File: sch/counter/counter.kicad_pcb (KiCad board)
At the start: 2 copper layers, 206 parts, among them J1 Q1, J10 ~CLK, J11 ~RST, J12 Cout, J13 ~Cout, J14 Vcc, J15 GND, J2 ~Q1, J3 Q2, J4 ~Q2, J5 Q4, J6 ~Q4, J7 Q8, J8 ~Q8, J9 CLK, Q1 Q_NMOS_GSD, Q10 Q_NMOS_GSD, Q11 Q_NMOS_GSD, Q12 Q_NMOS_GSD, Q13 Q_NMOS_GSD, Q14 Q_NMOS_GSD, Q15 Q_NMOS_GSD, Q16 Q_NMOS_GSD, Q17 Q_NMOS_GSD, Q18 Q_NMOS_GSD, Q19 Q_NMOS_GSD, Q2 Q_NMOS_GSD, Q20 Q_NMOS_GSD, Q21 Q_NMOS_GSD, Q22 Q_NMOS_GSD, Q23 Q_NMOS_GSD, Q24 Q_NMOS_GSD, Q25 Q_NMOS_GSD, Q26 Q_NMOS_GSD, Q27 Q_NMOS_GSD, Q28 Q_NMOS_GSD, Q29 Q_NMOS_GSD, Q3 Q_NMOS_GSD, Q30 Q_NMOS_GSD, Q31 Q_NMOS_GSD, Q32 Q_NMOS_GSD, Q33 Q_NMOS_GSD, Q34 Q_NMOS_GSD, Q35 Q_NMOS_GSD, Q4 Q_NMOS_GSD, Q5 Q_NMOS_GSD, Q6 Q_NMOS_GSD, Q7 Q_NMOS_GSD, Q8 Q_NMOS_GSD, Q9 Q_NMOS_GSD

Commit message: The counter board is complete
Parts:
- removed D93, D94, D95, D96: D, Diode_SMD:D_MiniMELF
- removed JP1, JP2, JP3, JP4: Jumper_3_Open, Connector_PinHeader_2.54mm:PinHeader_1x03_P2.54mm_Vertical
- added REF**: MountingHole_3.2mm_M3_DIN965_Pad, MountingHole:MountingHole_3.2mm_M3_DIN965_Pad, F.Cu at (149.0, 112.0)
- added REF**: MountingHole_3.2mm_M3_DIN965_Pad, MountingHole:MountingHole_3.2mm_M3_DIN965_Pad, F.Cu at (149.0, 29.0)
- added REF**: MountingHole_3.2mm_M3_DIN965_Pad, MountingHole:MountingHole_3.2mm_M3_DIN965_Pad, F.Cu at (104.0, 29.0)
- added REF**: MountingHole_3.2mm_M3_DIN965_Pad, MountingHole:MountingHole_3.2mm_M3_DIN965_Pad, F.Cu at (104.0, 112.0)
- moved Q33 304.7 mm to (113.3, 110.7)
- moved D98 300.0 mm to (118.4, 112.5)
- moved D97 299.4 mm to (118.4, 109.7)
- moved D87 298.6 mm to (113.8, 105.4), turned to 270 degrees
- moved D88 296.3 mm to (111.3, 105.4), turned to 270 degrees
- moved D86 296.1 mm to (106.2, 105.4), turned to 270 degrees
- moved D90 295.6 mm to (116.3, 105.4), turned to 270 degrees
- moved D89 293.3 mm to (118.9, 105.4), turned to 270 degrees
- moved D92 291.5 mm to (121.4, 105.4), turned to 270 degrees
- moved D85 288.0 mm to (108.7, 105.4), turned to 270 degrees
- moved R37 285.6 mm to (126.2, 106.2), turned to 270 degrees
- moved D49 281.0 mm to (104.1, 78.7)
- moved R22 279.0 mm to (108.6, 77.5), turned to 180 degrees
- moved R30 279.0 mm to (108.6, 95.2), turned to 180 degrees
- moved D91 278.2 mm to (124.0, 105.4), turned to 270 degrees
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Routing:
- net GND: track 0.00 -> 379.2 mm, vias 0 -> 36
- net VCC: track 0.00 -> 374.1 mm, vias 0 -> 37
- net /~ARST: track 0.00 -> 316.4 mm, vias 0 -> 21
- net /~Q1: track 26.7 -> 233.8 mm, vias 0 -> 5
- net /Q1: track 9.15 -> 211.5 mm, vias 0 -> 3
- net /~Q2: track 0.00 -> 198.9 mm, vias 0 -> 5
- net /Q2: track 0.00 -> 184.5 mm, vias 0 -> 3
- net /~Q4: track 0.00 -> 168.6 mm, vias 0 -> 5
- net /Q4: track 0.00 -> 159.2 mm, vias 0 -> 3
- net /~Q8: track 0.00 -> 111.2 mm, vias 0 -> 3
- net /Q8: track 0.00 -> 85.2 mm
- net Net-(D71-Pad1): track 0.00 -> 26.5 mm
- net Net-(C3-Pad1): track 0.00 -> 26.5 mm
- net Net-(D31-Pad1): track 0.00 -> 26.4 mm
- net Net-(D51-Pad1): track 0.00 -> 25.9 mm
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- added copper zone on F.Cu, net GND
- added copper zone on B.Cu, net VCC
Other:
- net class Default: clearance 0.2 -> 0.25
- rule trace_clearance: 0.2 -> 0.25

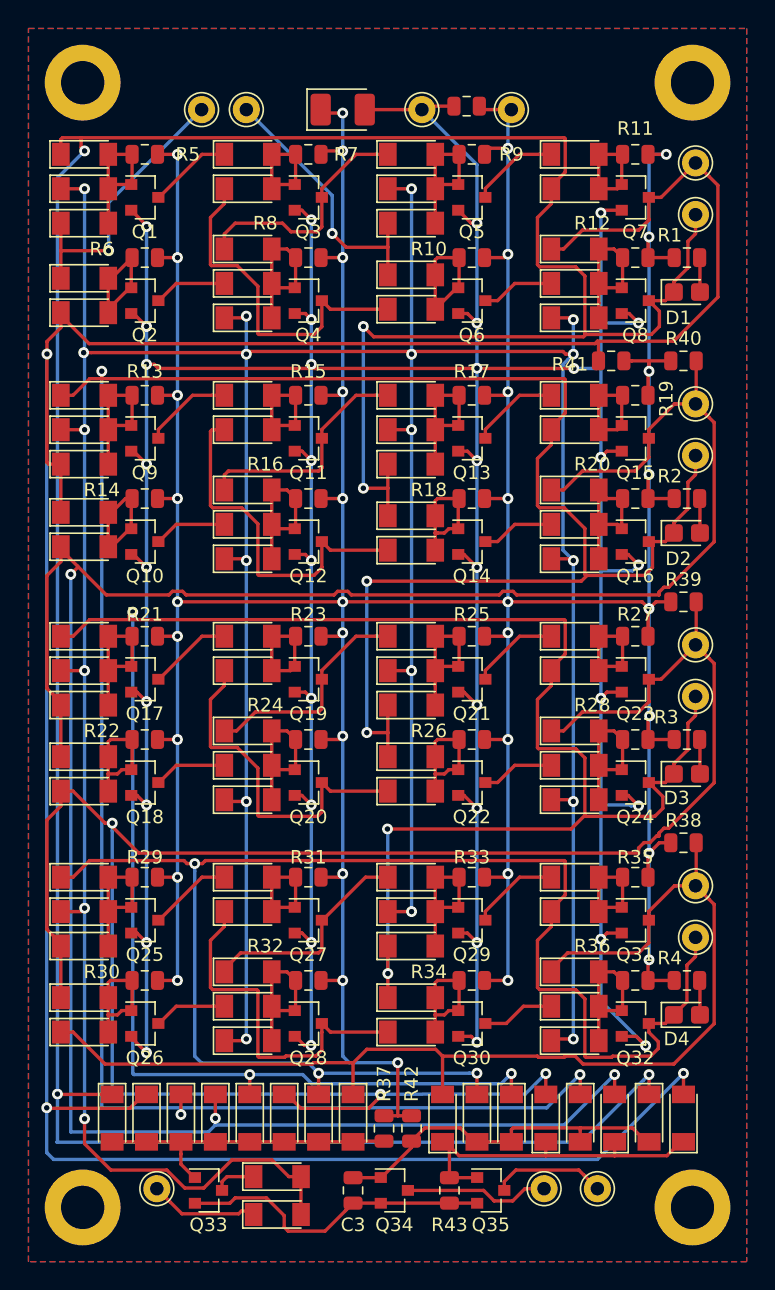
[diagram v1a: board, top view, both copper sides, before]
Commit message: Board modified: connectors used
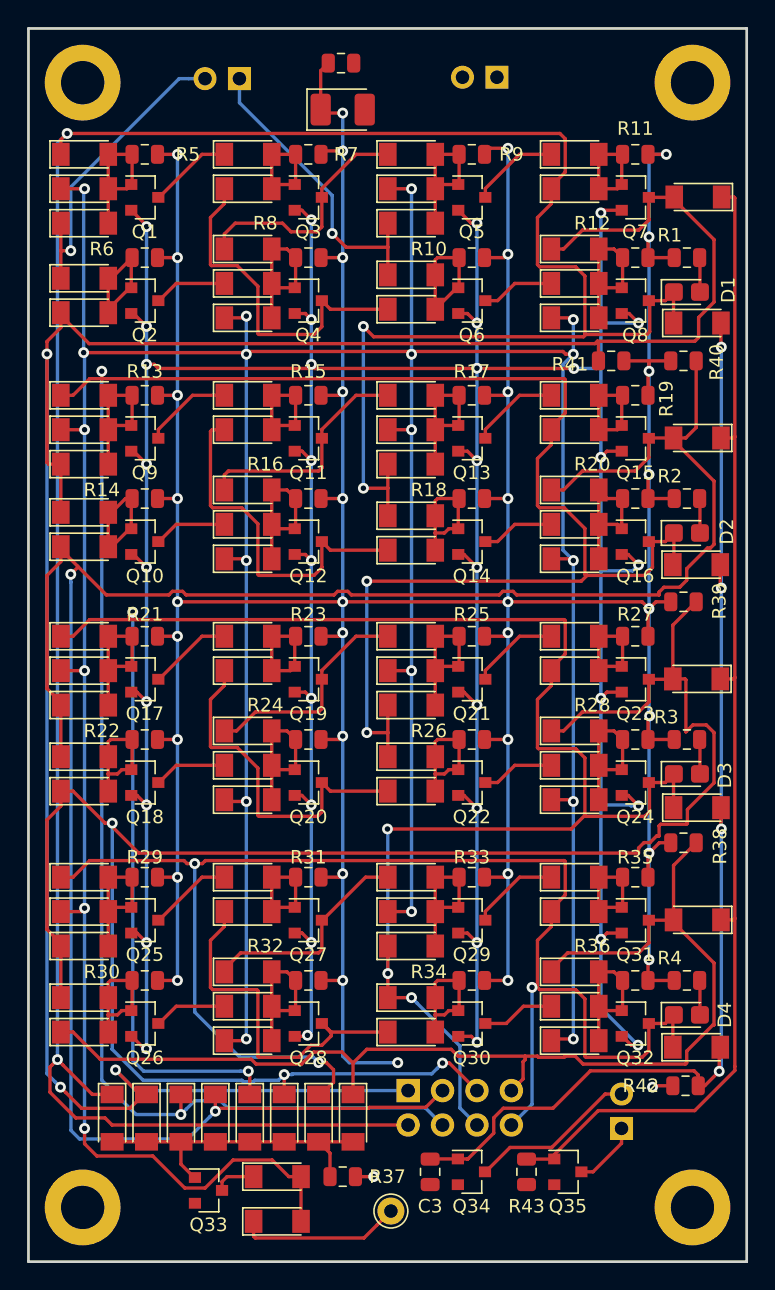
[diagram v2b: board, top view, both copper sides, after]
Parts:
- removed J10: ~CLK, Connector_Pin:Pin_D1.0mm_L10.0mm
- removed J12: Cout, Connector_Pin:Pin_D1.0mm_L10.0mm
- removed J13: ~Cout, Connector_Pin:Pin_D1.0mm_L10.0mm
- removed J14: Vcc, Connector_Pin:Pin_D1.0mm_L10.0mm
- removed J15: GND, Connector_Pin:Pin_D1.0mm_L10.0mm
- removed J5: Q4, Connector_Pin:Pin_D1.0mm_L10.0mm
- removed J6: ~Q4, Connector_Pin:Pin_D1.0mm_L10.0mm
- removed J7: Q8, Connector_Pin:Pin_D1.0mm_L10.0mm
- removed J8: ~Q8, Connector_Pin:Pin_D1.0mm_L10.0mm
- removed J9: CLK, Connector_Pin:Pin_D1.0mm_L10.0mm
- J1: value Q1 -> CLK; footprint Connector_Pin:Pin_D1.0mm_L10.0mm -> Connector_PinHeader_2.54mm:PinHeader_1x02_P2.54mm_Vertical; moved to B.Cu
- J2: value ~Q1 -> Carry; footprint Connector_Pin:Pin_D1.0mm_L10.0mm -> Connector_PinHeader_2.54mm:PinHeader_1x02_P2.54mm_Vertical; moved to B.Cu
- J3: value Q2 -> Power; footprint Connector_Pin:Pin_D1.0mm_L10.0mm -> Connector_PinHeader_2.54mm:PinHeader_1x02_P2.54mm_Vertical; moved to B.Cu
- J4: value ~Q2 -> Q; footprint Connector_Pin:Pin_D1.0mm_L10.0mm -> Connector_IDC:IDC-Header_2x04_P2.54mm_Vertical; moved to B.Cu
- moved D103 68.0 mm to (149.4, 37.4), turned to 180 degrees
- moved J2 67.7 mm to (143.8, 106.2)
- moved D99 58.8 mm to (149.4, 46.7), turned to 0 degrees
- moved J4 51.4 mm to (128.0, 103.4), turned to 270 degrees
- moved D104 50.6 mm to (149.4, 55.2), turned to 180 degrees
- moved D100 41.7 mm to (149.3, 64.6), turned to 0 degrees
- moved D105 34.3 mm to (149.3, 73.0), turned to 180 degrees
- moved J1 34.2 mm to (115.6, 28.7), turned to 90 degrees
- moved J3 28.2 mm to (134.6, 28.6), turned to 90 degrees
- moved D101 26.7 mm to (149.4, 82.5), turned to 0 degrees
- moved D106 23.8 mm to (149.4, 90.8), turned to 180 degrees
- moved R42 20.5 mm to (148.5, 103.0), turned to 0 degrees
- moved J11 17.4 mm to (126.7, 112.3)
- moved D102 17.0 mm to (149.3, 100.2), turned to 0 degrees
- moved C1 9.80 mm to (123.1, 27.6), turned to 0 degrees
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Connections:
- J1 pad 1: /Q1 -> /CLK
- J2 pad 1: /~Q1 -> /Cout
- J3 pad 1: /Q2 -> VCC
- J4 pad 1: /~Q2 -> /Q1
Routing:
- net Net-(D103-Pad1): track 25.6 -> 86.9 mm
- net Net-(C3-Pad1): track 26.5 -> 86.5 mm, vias 0 -> 4
- net GND: track 379.2 -> 336.7 mm
- net /Q1: track 211.5 -> 176.8 mm
- net /~Q1: track 233.8 -> 206.7 mm, vias 5 -> 4
- net /~Q2: track 198.9 -> 181.9 mm, vias 5 -> 4
- net /Q2: track 184.5 -> 168.6 mm, vias 3 -> 2
- net /~Q4: track 168.6 -> 154.7 mm
- net /Q4: track 159.2 -> 146.3 mm
- net /~Q8: track 111.2 -> 104.3 mm
- net /~RSTin: track 7.99 -> 12.8 mm
- net VCC: track 374.1 -> 369.3 mm, vias 37 -> 39
- net /Cout: track 8.45 -> 4.93 mm
- net /CLK: track 20.1 -> 22.6 mm
- net /~CLK: track 20.8 -> 22.9 mm
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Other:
- board outline added: 53 x 91 mm

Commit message: Modified the counter board
Added mounting holes to the schematics
Changed reset connector to have 2 pins
Added labels for connectors and configuration diodes
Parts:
- removed J11: ~RST, Connector_Pin:Pin_D1.0mm_L10.0mm
- removed REF** (x4): MountingHole_3.2mm_M3_DIN965_Pad, MountingHole:MountingHole_3.2mm_M3_DIN965_Pad
- added H1: MountingHole_Pad, MountingHole:MountingHole_3.2mm_M3_DIN965_Pad, F.Cu at (149.0, 112.0)
- added H2: MountingHole_Pad, MountingHole:MountingHole_3.2mm_M3_DIN965_Pad, F.Cu at (149.0, 29.0)
- added H3: MountingHole_Pad, MountingHole:MountingHole_3.2mm_M3_DIN965_Pad, F.Cu at (104.0, 29.0)
- added H4: MountingHole_Pad, MountingHole:MountingHole_3.2mm_M3_DIN965_Pad, F.Cu at (104.0, 112.0)
- added J5: ~RST, Connector_PinHeader_2.54mm:PinHeader_1x02_P2.54mm_Vertical, B.Cu at (124.5, 112.4)
- moved J3 2.49 mm to (132.1, 28.6), turned to 270 degrees
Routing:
- net GND: track 336.7 -> 362.8 mm, vias 36 -> 38
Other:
- board text added: "- +"
- board text added: "0"
- board text added: "1"
- board text added: "2"
- board text added: "4"
- board text added: "8"
- board text added: "CLK"
- board text added: "Carry"
- board text added: "Output"
- board text added: "~CLK"
- board text added: "~Carry"
- board text added: "~RST"

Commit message: Added bill of materials, modified counter PCB
Adjusted component positions for better GND filling
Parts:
- moved R26 0.43 mm to (132.8, 77.9)
- moved R18 0.41 mm to (132.8, 60.1)
- moved R14 0.41 mm to (108.6, 60.1)
- moved Q18 0.36 mm to (108.6, 81.0)
- moved Q10 0.34 mm to (108.6, 63.2)
- moved R22 0.33 mm to (108.6, 77.8)
- moved R6 0.29 mm to (108.6, 42.2)
- moved Q14 0.25 mm to (132.8, 63.1)
- moved Q2 0.21 mm to (108.6, 45.3)
- moved Q22 0.18 mm to (132.8, 80.8)
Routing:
- net GND: track 362.8 -> 351.0 mm, vias 38 -> 36
- net /Q2: track 168.6 -> 165.2 mm
- net /Q4: track 146.3 -> 144.0 mm
- net /Q1: track 176.8 -> 177.8 mm
